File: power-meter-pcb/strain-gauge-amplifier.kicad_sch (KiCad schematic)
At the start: 10 parts, among them J3 Side A, J5 Side B, U3 ADS1232IPW

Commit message: Assigning footprints, extremely rough idea of size
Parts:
- C3: footprint (none) -> Capacitor_SMD:C_0603_1608Metric_Pad1.08x0.95mm_HandSolder
- J3, J5: footprint (none) -> Connector_PinHeader_2.54mm:PinHeader_1x04_P2.54mm_Vertical
- U3: footprint (none) -> Package_SO:HTSSOP-24-1EP_4.4x7.8mm_P0.65mm_EP3.4x7.8mm_Mask2.4x4.68mm
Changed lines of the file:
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@@
 			)
 		)
-		(property "Footprint" ""
+		(property "Footprint" "Capacitor_SMD:C_0603_1608Metric_Pad1.08x0.95mm_HandSolder"
 			(at 153.3652 90.17 0)
 			(effects
@@
 			)
 		)
-		(property "Footprint" ""
+		(property "Footprint" "Connector_PinHeader_2.54mm:PinHeader_1x04_P2.54mm_Vertical"
 			(at 93.98 76.2 0)
 			(effects
@@
 			)
 		)
-		(property "Footprint" ""
+		(property "Footprint" "Connector_PinHeader_2.54mm:PinHeader_1x04_P2.54mm_Vertical"
 			(at 121.92 76.2 0)
 			(effects
@@
 			)
 		)
-		(property "Footprint" ""
+		(property "Footprint" "Package_SO:HTSSOP-24-1EP_4.4x7.8mm_P0.65mm_EP3.4x7.8mm_Mask2.4x4.68mm"
 			(at 181.61 97.79 0)
 			(effects

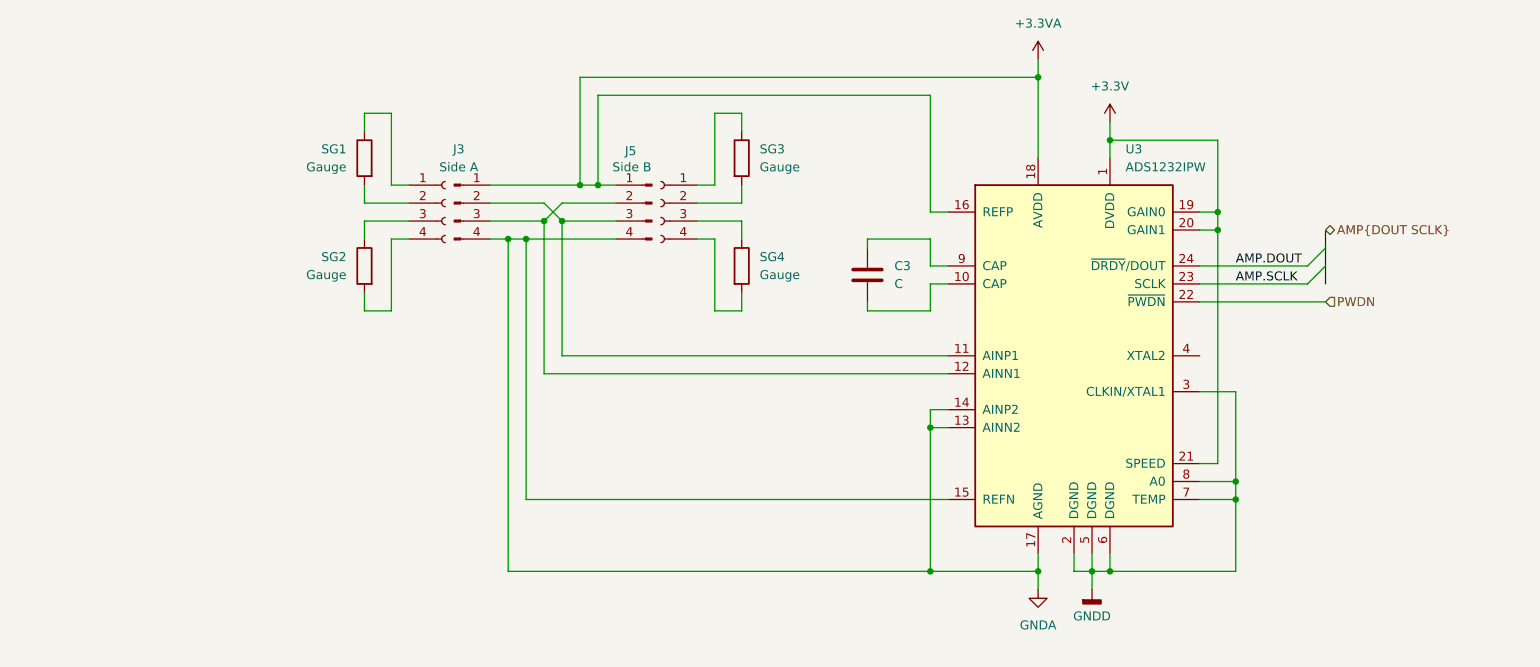
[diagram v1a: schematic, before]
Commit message: Added power supply to PCB
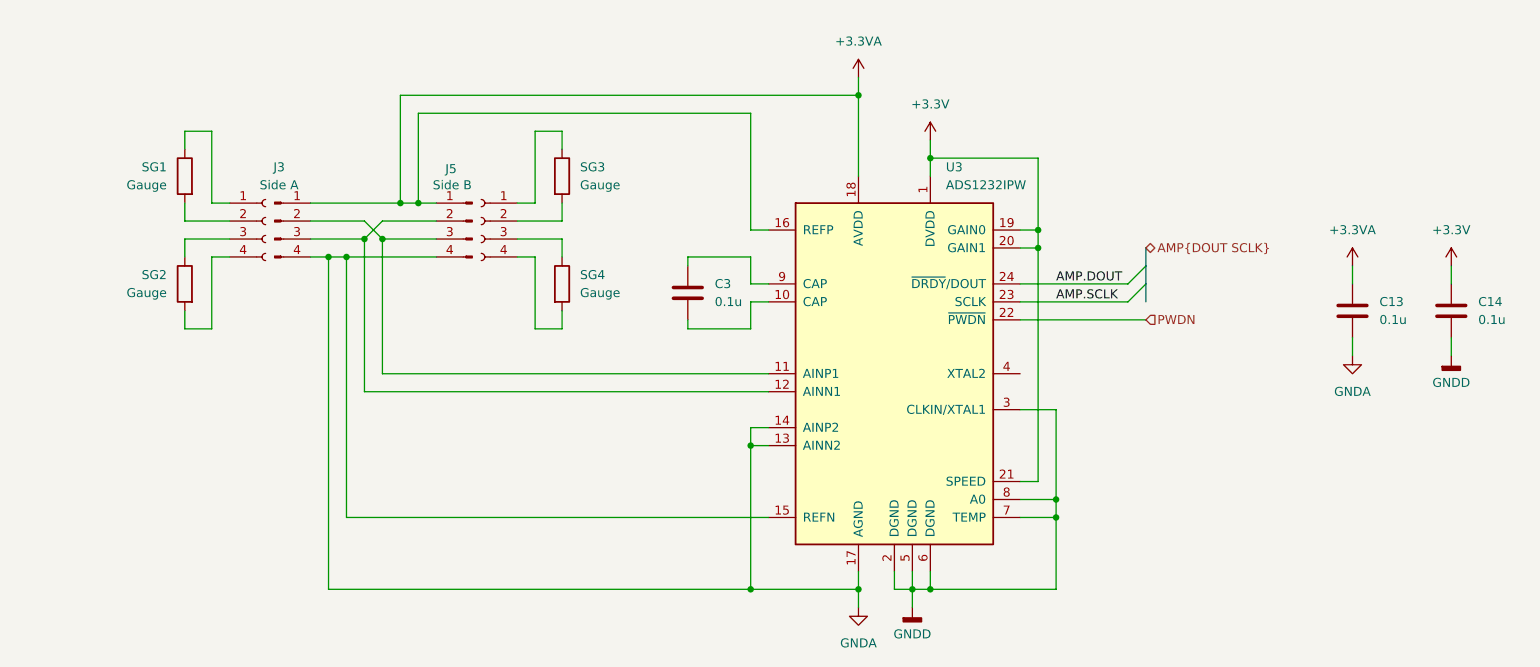
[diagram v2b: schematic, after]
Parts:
- added C13, C14: 0.1u, Capacitor_SMD:C_0603_1608Metric_Pad1.08x0.95mm_HandSolder, symbol Device:C
- C3: value C -> 0.1u
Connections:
- net +3.3V: now also C14.1
- net +3.3VA: now also C13.1
- net GNDA: now also C13.2
- net GNDD: now also C14.2
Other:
- moved on the sheet: C3, J3, J5, SG1, SG2, SG3, SG4, U3

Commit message: Started PCB layout
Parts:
- added NT1, NT3: NetTie_2, NetTie:NetTie-2_SMD_Pad0.5mm, symbol Device:NetTie_2
- added Q3: AS2302, Package_TO_SOT_SMD:TSOT-23, symbol Device:Q_NMOS_GSD
- added R13, R14, R15: 47, Resistor_SMD:R_0603_1608Metric_Pad0.98x0.95mm_HandSolder, symbol Device:R
- U7: renamed from U3; footprint Package_SO:HTSSOP-24-1EP_4.4x7.8mm_P0.65mm_EP3.4x7.8mm_Mask2.4x4.68mm -> Package_SO:TSSOP-24_4.4x7.8mm_P0.65mm
- renumbered #J4 to #J1, #J6 to #J2, C3 to C11, C13 to C12, C14 to C13, J3 to J4
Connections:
- net +3.3VA: now also NT3.1; no longer U7.16 (REFP)
- net AMP.DOUT: now also R13.2; no longer U7.24 (~{DRDY}/DOUT)
- net AMP.SCLK: now also R14.2; no longer U7.23 (SCLK)
- net GNDA: now also NT1.1, Q3.2 (S); no longer J4.4 (Pin_4), J5.4 (Pin_4), U7.15 (REFN)
- net GNDD: now also NT1.2
- net PWDN: now also Q3.1 (G), R15.2; no longer U7.22 (~{PWDN})
- net GA: now reaches J4.2 (Pin_2), J5.3 (Pin_3), U7.11 (AINP1)
- net GB: now reaches J4.3 (Pin_3), J5.2 (Pin_2), U7.12 (AINN1)
- new net: R13.1, U7.24 (~{DRDY}/DOUT)
- new net: R15.1, U7.22 (~{PWDN})
- new net: R14.1, U7.23 (SCLK)
- new net GN: J4.4 (Pin_4), J5.4 (Pin_4), Q3.3 (D), U7.15 (REFN)
- new net GP: NT3.2, U7.16 (REFP)
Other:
- moved on the sheet: C12

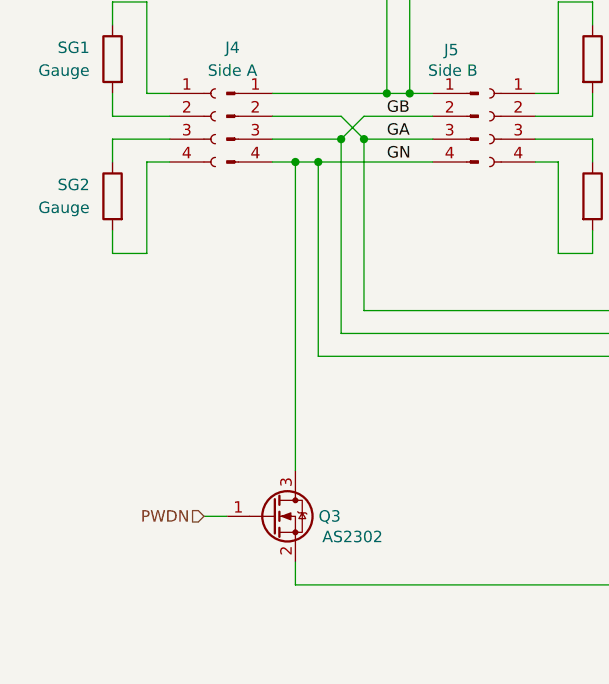
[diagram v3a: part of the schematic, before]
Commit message: Adding filtering and pullup resistors, board layout
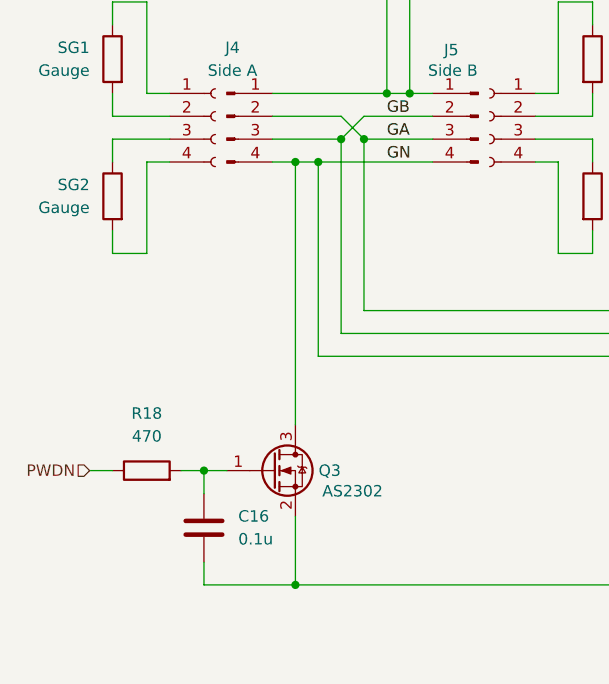
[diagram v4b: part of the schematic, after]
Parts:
- added C16: 0.1u, Capacitor_SMD:C_0603_1608Metric_Pad1.08x0.95mm_HandSolder, symbol Device:C
- added R18: 470, Resistor_SMD:R_0603_1608Metric_Pad0.98x0.95mm_HandSolder, symbol Device:R
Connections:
- net GNDA: now also C16.2
- net PWDN: now also R18.1; no longer Q3.1 (G)
- new net: C16.1, Q3.1 (G), R18.2
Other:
- moved on the sheet: Q3
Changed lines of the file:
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@@
+	)
+	(junction
+		(at 66.04 118.11)
+		(diameter 0)
+		(color 0 0 0 0)
 	)
 	(junction
@@
 	)
 	(junction
+		(at 76.2 130.81)
+		(diameter 0)
+		(color 0 0 0 0)
+	)
+	(junction
 		(at 176.53 82.55)
 		(diameter 0)
@@
 	(wire
 		(pts
-			(xy 76.2 118.11) (xy 76.2 83.82)
+			(xy 76.2 113.03) (xy 76.2 83.82)
 		)
 		(stroke
@@
 	(wire
 		(pts
-			(xy 66.04 123.19) (xy 68.58 123.19)
-		)
-		(stroke
-			(width 0)
-			(type default)
-		)
-	)
-	(wire
-		(pts
 			(xy 138.43 107.95) (xy 135.89 107.95)
 		)
@@
 	(wire
 		(pts
+			(xy 63.5 118.11) (xy 66.04 118.11)
+		)
+		(stroke
+			(width 0)
+			(type default)
+		)
+	)
+	(wire
+		(pts
+			(xy 66.04 118.11) (xy 66.04 120.65)
+		)
+		(stroke
+			(width 0)
+			(type default)
+		)
+	)
+	(wire
+		(pts
+			(xy 53.34 118.11) (xy 55.88 118.11)
+		)
+		(stroke
+			(width 0)
+			(type default)
+		)
+	)
+	(wire
+		(pts
 			(xy 173.99 80.01) (xy 176.53 80.01)
 		)
@@
 	(wire
 		(pts
+			(xy 66.04 118.11) (xy 68.58 118.11)
+		)
+		(stroke
+			(width 0)
+			(type default)
+		)
+	)
+	(wire
+		(pts
 			(xy 86.36 60.96) (xy 151.13 60.96)
 		)
@@
 	(wire
 		(pts
+			(xy 66.04 128.27) (xy 66.04 130.81)
+		)
+		(stroke
+			(width 0)
+			(type default)
+		)
+	)
+	(wire
+		(pts
 			(xy 78.74 105.41) (xy 78.74 83.82)
 		)
@@
 	(wire
 		(pts
-			(xy 76.2 130.81) (xy 76.2 128.27)
+			(xy 76.2 130.81) (xy 76.2 123.19)
 		)
 		(stroke
@@
 		(pts
 			(xy 73.66 81.28) (xy 81.28 81.28)
+		)
+		(stroke
+			(width 0)
+			(type default)
+		)
+	)
+	(wire
+		(pts
+			(xy 66.04 130.81) (xy 76.2 130.81)
 		)
 		(stroke
@@
 	(hierarchical_label "PWDN"
 		(shape input)
-		(at 66.04 123.19 180)
+		(at 53.34 118.11 180)
 		(fields_autoplaced yes)
 		(effects
@@
 	)
 	(symbol
+		(lib_id "Device:C")
+		(at 66.04 124.46 0)
+		(unit 1)
+		(exclude_from_sim no)
+		(in_bom yes)
+		(on_board yes)
+		(dnp no)
+		(fields_autoplaced yes)
+		(property "Reference" "C16"
+			(at 69.85 123.1899 0)
+			(effects
+				(font
+					(size 1.27 1.27)
+				)
+				(justify left)
+			)
+		)
+		(property "Value" "0.1u"
+			(at 69.85 125.7299 0)
+			(effects
+				(font
+					(size 1.27 1.27)
+				)
+				(justify left)
+			)
+		)
+		(property "Footprint" "Capacitor_SMD:C_0603_1608Metric_Pad1.08x0.95mm_HandSolder"
+			(at 67.0052 128.27 0)
+			(effects
+				(font
+					(size 1.27 1.27)
+				)
+				(hide yes)
+			)
+		)
+		(property "Datasheet" "~"
+			(at 66.04 124.46 0)
+			(effects
+				(font
+					(size 1.27 1.27)
+				)
+				(hide yes)
+			)
+		)
+		(property "Description" "Unpolarized capacitor"
+			(at 66.04 124.46 0)
+			(effects
+				(font
+					(size 1.27 1.27)
+				)
+				(hide yes)
+			)
+		)
+		(pin "1"
+		)
+		(pin "2"
+		)
+		(instances
+			(project "power-meter-pcb"
+				(path "/73d1dc3f-3725-4767-8c11-2d32e15ee0d6/feb88761-b4a9-421c-bc5f-37e5e311e229"
+					(reference "C16")
+					(unit 1)
+				)
+			)
+		)
+	)
+	(symbol
 		(lib_id "Device:R")
 		(at 109.22 87.63 0)
@@
 	)
 	(symbol
+		(lib_id "Device:R")
+		(at 59.69 118.11 90)
+		(unit 1)
+		(exclude_from_sim no)
+		(in_bom yes)
+		(on_board yes)
+		(dnp no)
+		(fields_autoplaced yes)
+		(property "Reference" "R18"
+			(at 59.69 111.76 90)
+			(effects
+				(font
+					(size 1.27 1.27)
+				)
+			)
+		)
+		(property "Value" "470"
+			(at 59.69 114.3 90)
+			(effects
+				(font
+					(size 1.27 1.27)
+				)
+			)
+		)
+		(property "Footprint" "Resistor_SMD:R_0603_1608Metric_Pad0.98x0.95mm_HandSolder"
+			(at 59.69 119.888 90)
+			(effects
+				(font
+					(size 1.27 1.27)
+				)
+				(hide yes)
+			)
+		)
+		(property "Datasheet" "~"
+			(at 59.69 118.11 0)
+			(effects
+				(font
+					(size 1.27 1.27)
+				)
+				(hide yes)
+			)
+		)
+		(property "Description" "Resistor"
+			(at 59.69 118.11 0)
+			(effects
+				(font
+					(size 1.27 1.27)
+				)
+				(hide yes)
+			)
+		)
+		(pin "1"
+		)
+		(pin "2"
+		)
+		(instances
+			(project "power-meter-pcb"
+				(path "/73d1dc3f-3725-4767-8c11-2d32e15ee0d6/feb88761-b4a9-421c-bc5f-37e5e311e229"
+					(reference "R18")
+					(unit 1)
+				)
+			)
+		)
+	)
+	(symbol
 		(lib_id "power:+3.3VA")
 		(at 151.13 58.42 0)
@@
 	(symbol
 		(lib_id "Device:Q_NMOS_GSD")
-		(at 73.66 123.19 0)
+		(at 73.66 118.11 0)
 		(unit 1)
 		(exclude_from_sim no)
@@
 		(dnp no)
 		(property "Reference" "Q3"
-			(at 80.01 123.19 0)
+			(at 80.01 118.11 0)
 			(effects
 				(font
@@
 		)
 		(property "Value" "AS2302"
-			(at 82.55 125.476 0)
+			(at 82.55 120.396 0)
 			(effects
 				(font
@@
 		)
 		(property "Footprint" "Package_TO_SOT_SMD:TSOT-23"
-			(at 78.74 120.65 0)
+			(at 78.74 115.57 0)
 			(effects
 				(font
@@
 		)
 		(property "Datasheet" "~"
-			(at 73.66 123.19 0)
+			(at 73.66 118.11 0)
 			(effects
 				(font
@@
 		)
 		(property "Description" "N-MOSFET transistor, gate/source/drain"
-			(at 73.66 123.19 0)
-			(effects
-				(font
+			(at 73.66 118.11 0)
+			(effects
+				(font

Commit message: Routing and component placement continues
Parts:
- renumbered C16 to C12, C11 to C13, C12 to C14, C13 to C15, J4 to J5, J5 to J6, NT3 to NT1, NT1 to NT2, R18 to R16, R13 to R17, R14 to R18, R15 to R19
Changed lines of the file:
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@@
+		)
+	)
+	(bus
+		(pts
+			(xy 203.2 87.63) (xy 203.2 88.9)
+		)
+		(stroke
+			(width 0)
+			(type default)
 		)
 	)
@@
 		(pts
 			(xy 62.23 81.28) (xy 55.88 81.28)
-		)
-		(stroke
-			(width 0)
-			(type default)
-		)
-	)
-	(bus
-		(pts
-			(xy 203.2 87.63) (xy 203.2 90.17)
 		)
 		(stroke
@@
 		(dnp no)
 		(fields_autoplaced yes)
-		(property "Reference" "#PWR035"
+		(property "Reference" "#PWR037"
 			(at 161.29 71.12 0)
 			(effects
@@
 			(project "power-meter-pcb"
 				(path "/73d1dc3f-3725-4767-8c11-2d32e15ee0d6/feb88761-b4a9-421c-bc5f-37e5e311e229"
-					(reference "#PWR035")
+					(reference "#PWR037")
 					(unit 1)
 				)
@@
 		(dnp no)
 		(fields_autoplaced yes)
-		(property "Reference" "#PWR033"
+		(property "Reference" "#PWR035"
 			(at 151.13 139.7 0)
 			(effects
@@
 			(project "power-meter-pcb"
 				(path "/73d1dc3f-3725-4767-8c11-2d32e15ee0d6/feb88761-b4a9-421c-bc5f-37e5e311e229"
-					(reference "#PWR033")
+					(reference "#PWR035")
 					(unit 1)
 				)
@@
 		(dnp no)
 		(fields_autoplaced yes)
-		(property "Reference" "#PWR036"
+		(property "Reference" "#PWR038"
 			(at 224.79 88.9 0)
 			(effects
@@
 			(project "power-meter-pcb"
 				(path "/73d1dc3f-3725-4767-8c11-2d32e15ee0d6/feb88761-b4a9-421c-bc5f-37e5e311e229"
-					(reference "#PWR036")
+					(reference "#PWR038")
 					(unit 1)
 				)
@@
 		(dnp no)
 		(fields_autoplaced yes)
-		(property "Reference" "R13"
+		(property "Reference" "R17"
 			(at 185.42 81.28 90)
 			(effects
@@
 			(project "power-meter-pcb"
 				(path "/73d1dc3f-3725-4767-8c11-2d32e15ee0d6/feb88761-b4a9-421c-bc5f-37e5e311e229"
-					(reference "R13")
+					(reference "R17")
 					(unit 1)
 				)
@@
 		(dnp no)
 		(fields_autoplaced yes)
-		(property "Reference" "C16"
+		(property "Reference" "C12"
 			(at 69.85 123.1899 0)
 			(effects
@@
 			(project "power-meter-pcb"
 				(path "/73d1dc3f-3725-4767-8c11-2d32e15ee0d6/feb88761-b4a9-421c-bc5f-37e5e311e229"
-					(reference "C16")
+					(reference "C12")
 					(unit 1)
 				)
@@
 		(on_board yes)
 		(dnp no)
-		(property "Reference" "R15"
+		(property "Reference" "R19"
 			(at 185.42 100.584 90)
 			(effects
@@
 			(project "power-meter-pcb"
 				(path "/73d1dc3f-3725-4767-8c11-2d32e15ee0d6/feb88761-b4a9-421c-bc5f-37e5e311e229"
-					(reference "R15")
+					(reference "R19")
 					(unit 1)
 				)
@@
 		(dnp no)
 		(fields_autoplaced yes)
-		(property "Reference" "C11"
+		(property "Reference" "C13"
 			(at 130.81 87.6299 0)
 			(effects
@@
 			(project "power-meter-pcb"
 				(path "/73d1dc3f-3725-4767-8c11-2d32e15ee0d6/feb88761-b4a9-421c-bc5f-37e5e311e229"
-					(reference "C11")
+					(reference "C13")
 					(unit 1)
 				)
@@
 		(dnp no)
 		(fields_autoplaced yes)
-		(property "Reference" "J4"
+		(property "Reference" "J5"
 			(at 69.215 71.12 0)
 			(effects
@@
 			(project "power-meter-pcb"
 				(path "/73d1dc3f-3725-4767-8c11-2d32e15ee0d6/feb88761-b4a9-421c-bc5f-37e5e311e229"
-					(reference "J4")
+					(reference "J5")
 					(unit 1)
 				)
@@
 		(dnp no)
 		(fields_autoplaced yes)
-		(property "Reference" "NT1"
+		(property "Reference" "NT2"
 			(at 153.67 128.27 0)
 			(effects
@@
 			(project "power-meter-pcb"
 				(path "/73d1dc3f-3725-4767-8c11-2d32e15ee0d6/feb88761-b4a9-421c-bc5f-37e5e311e229"
-					(reference "NT1")
+					(reference "NT2")
 					(unit 1)
 				)
@@
 		(dnp no)
 		(fields_autoplaced yes)
-		(property "Reference" "C13"
+		(property "Reference" "C15"
 			(at 238.76 90.1699 0)
 			(effects
@@
 			(project "power-meter-pcb"
 				(path "/73d1dc3f-3725-4767-8c11-2d32e15ee0d6/feb88761-b4a9-421c-bc5f-37e5e311e229"
-					(reference "C13")
+					(reference "C15")
 					(unit 1)
 				)
@@
 		(dnp no)
 		(fields_autoplaced yes)
-		(property "Reference" "C12"
+		(property "Reference" "C14"
 			(at 228.6 90.1699 0)
 			(effects
@@
 			(project "power-meter-pcb"
 				(path "/73d1dc3f-3725-4767-8c11-2d32e15ee0d6/feb88761-b4a9-421c-bc5f-37e5e311e229"
-					(reference "C12")
+					(reference "C14")
 					(unit 1)
 				)
@@
 		(on_board yes)
 		(dnp no)
-		(property "Reference" "J5"
+		(property "Reference" "J6"
 			(at 92.71 71.374 0)
 			(effects
@@
 			(project "power-meter-pcb"
 				(path "/73d1dc3f-3725-4767-8c11-2d32e15ee0d6/feb88761-b4a9-421c-bc5f-37e5e311e229"
-					(reference "J5")
+					(reference "J6")
 					(unit 1)
 				)
@@
 		(on_board yes)
 		(dnp no)
-		(property "Reference" "NT3"
+		(property "Reference" "NT1"
 			(at 127 65.786 0)
 			(effects
@@
 			(project "power-meter-pcb"
 				(path "/73d1dc3f-3725-4767-8c11-2d32e15ee0d6/feb88761-b4a9-421c-bc5f-37e5e311e229"
-					(reference "NT3")
+					(reference "NT1")
 					(unit 1)
 				)
@@
 		(dnp no)
 		(fields_autoplaced yes)
-		(property "Reference" "R18"
+		(property "Reference" "R16"
 			(at 59.69 111.76 90)
 			(effects
@@
 			(project "power-meter-pcb"
 				(path "/73d1dc3f-3725-4767-8c11-2d32e15ee0d6/feb88761-b4a9-421c-bc5f-37e5e311e229"
-					(reference "R18")
+					(reference "R16")
 					(unit 1)
 				)
@@
 		(dnp no)
 		(fields_autoplaced yes)
-		(property "Reference" "#PWR032"
+		(property "Reference" "#PWR034"
 			(at 151.13 62.23 0)
 			(effects
@@
 			(project "power-meter-pcb"
 				(path "/73d1dc3f-3725-4767-8c11-2d32e15ee0d6/feb88761-b4a9-421c-bc5f-37e5e311e229"
-					(reference "#PWR032")
+					(reference "#PWR034")
 					(unit 1)
 				)
@@
 		(dnp no)
 		(fields_autoplaced yes)
-		(property "Reference" "#PWR037"
+		(property "Reference" "#PWR039"
 			(at 224.79 104.14 0)
 			(effects
@@
 			(project "power-meter-pcb"
 				(path "/73d1dc3f-3725-4767-8c11-2d32e15ee0d6/feb88761-b4a9-421c-bc5f-37e5e311e229"
-					(reference "#PWR037")
+					(reference "#PWR039")
 					(unit 1)
 				)
@@
 		(dnp no)
 		(fields_autoplaced yes)
-		(property "Reference" "#PWR039"
+		(property "Reference" "#PWR041"
 			(at 234.95 104.14 0)
 			(effects
@@
 			(project "power-meter-pcb"
 				(path "/73d1dc3f-3725-4767-8c11-2d32e15ee0d6/feb88761-b4a9-421c-bc5f-37e5e311e229"
-					(reference "#PWR039")
+					(reference "#PWR041")
 					(unit 1)
 				)
@@
 		(dnp no)
 		(fields_autoplaced yes)
-		(property "Reference" "#PWR038"
+		(property "Reference" "#PWR040"
 			(at 234.95 88.9 0)
 			(effects
@@
 			(project "power-meter-pcb"
 				(path "/73d1dc3f-3725-4767-8c11-2d32e15ee0d6/feb88761-b4a9-421c-bc5f-37e5e311e229"
-					(reference "#PWR038")
+					(reference "#PWR040")
 					(unit 1)
 				)
@@
 		(on_board yes)
 		(dnp no)
-		(property "Reference" "R14"
+		(property "Reference" "R18"
 			(at 185.42 92.964 90)
 			(effects
@@
 			(project "power-meter-pcb"
 				(path "/73d1dc3f-3725-4767-8c11-2d32e15ee0d6/feb88761-b4a9-421c-bc5f-37e5e311e229"
-					(reference "R14")
+					(reference "R18")
 					(unit 1)
 				)
@@
 		(dnp no)
 		(fields_autoplaced yes)
-		(property "Reference" "#PWR034"
+		(property "Reference" "#PWR036"
 			(at 158.75 139.7 0)
 			(effects
@@
 			(project "power-meter-pcb"
 				(path "/73d1dc3f-3725-4767-8c11-2d32e15ee0d6/feb88761-b4a9-421c-bc5f-37e5e311e229"
-					(reference "#PWR034")
+					(reference "#PWR036")
 					(unit 1)
 				)
